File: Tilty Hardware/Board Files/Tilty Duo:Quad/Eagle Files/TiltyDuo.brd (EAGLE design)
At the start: 38.1 x 50.8 mm, 36 parts, among them U1 HMC5883LSMD, U2 HC-09_BREAKOUT, U3 MPL3115A2LGA8, U4 LM2931, U5 MPU-6050

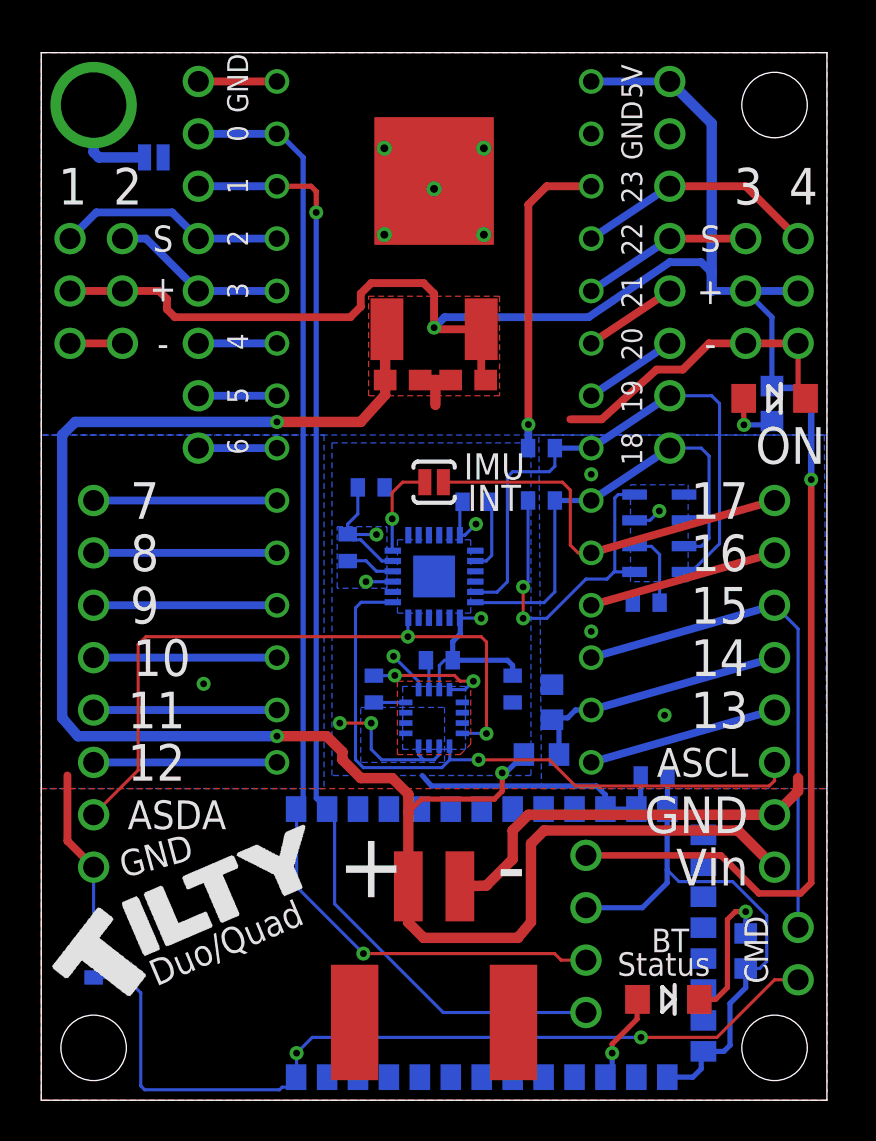
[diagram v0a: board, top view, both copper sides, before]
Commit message: Final prototype Tilty Duo/Quad PCB and BOM
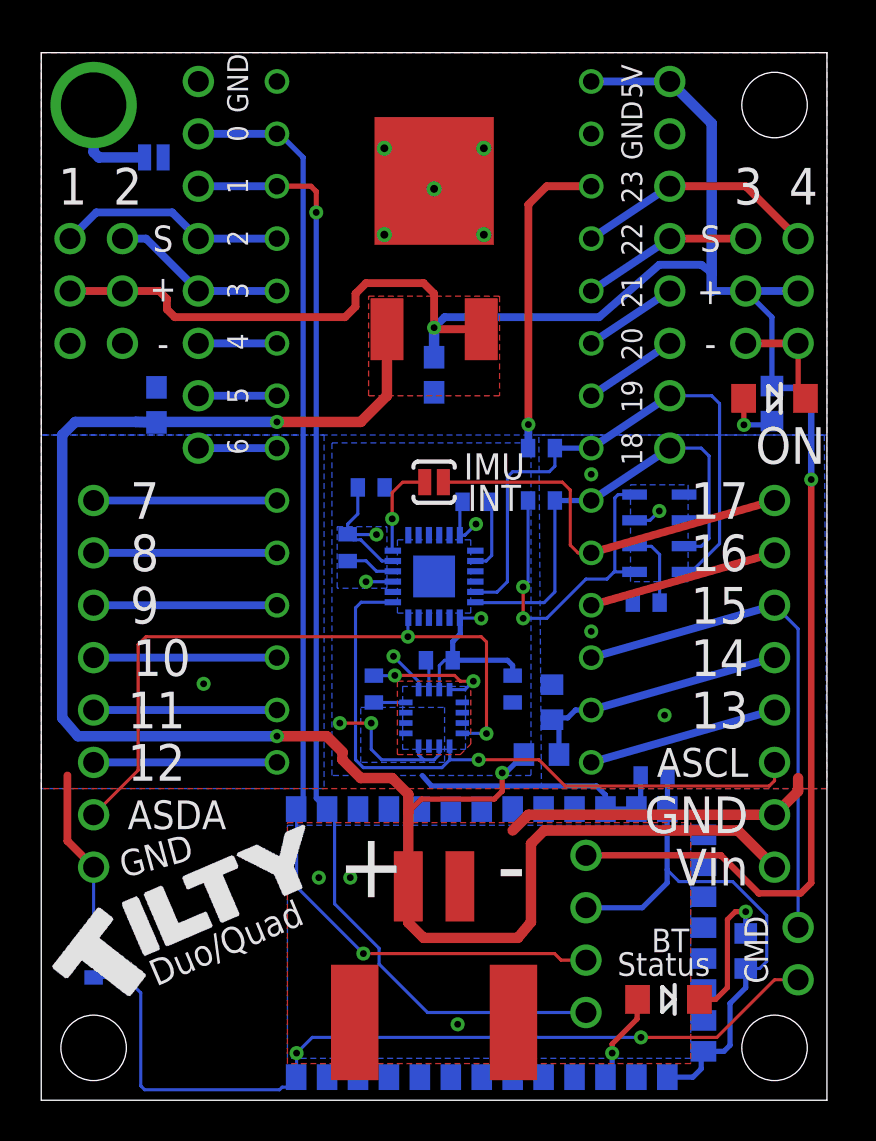
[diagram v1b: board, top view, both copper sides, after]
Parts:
- moved C4 12.0 mm to (5.59, 33.7), flipped to the bottom, turned to 90 degrees
- moved C5 1.67 mm to (19.1, 35.2), flipped to the bottom, turned to 270 degrees
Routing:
- net GND: track 108.3 -> 84.8 mm, vias 15 -> 18
- net 5V: track 102.8 -> 101.6 mm
- net VBATT: track 88.8 -> 90.0 mm
- removed copper zone on layer 1, net N$25

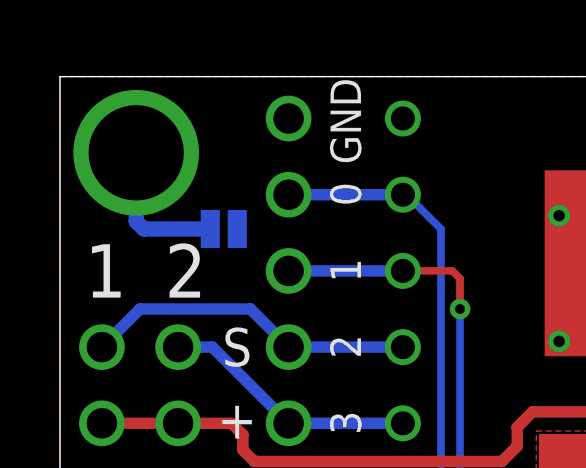
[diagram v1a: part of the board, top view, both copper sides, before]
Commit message: Added Bottom layer solder stencil for Duo/Quad board
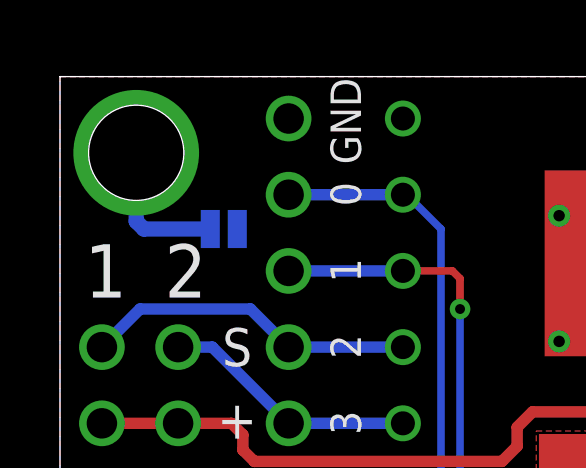
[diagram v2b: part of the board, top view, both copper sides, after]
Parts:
- removed U$1: TEENSY_3.0_OUTER-PINS28-DIP_SOCKET, My Parts:28-DIP
- added U6: HMC5883LSMD, SparkFun:16LPCC
- U1: value HMC5883LSMD -> TEENSY_3.0_OUTER-PINS28-DIP_SOCKET; device SparkFun:16LPCC -> My Parts:28-DIP
- moved U1 14.4 mm to (19.1, 32.9), flipped to the top, turned to 0 degrees
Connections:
- net 5V: now also U1.P$15; no longer U$1.P$15
- net AGND: now also U1.P$16; no longer U$1.P$16
- net AUXCL: now also U6.1; no longer U1.1
- net AUXDA: now also U6.16; no longer U1.16
- net BATT_SENSE: now also U1.P$27; no longer U$1.P$27
- net BT_CMD: now also U1.P$26; no longer U$1.P$26
- net GND: now also U1.P$1, U6.11, U6.9; no longer U$1.P$1, U1.11, U1.9
- net I/O1: now also U1.P$4; no longer U$1.P$4
- net I/O2: now also U1.P$5; no longer U$1.P$5
- net I/O3: now also U1.P$18; no longer U$1.P$18
- net I/O4: now also U1.P$19; no longer U$1.P$19
- net MPU_INT: now also U1.P$24; no longer U$1.P$24
- net N$10: now also U1.P$28; no longer U$1.P$28
- net N$11: now also U6.10; no longer U1.10
- net N$12: now also U1.P$11; no longer U$1.P$11
- net N$13: now also U1.P$12; no longer U$1.P$12
- net N$14: now also U1.P$13; no longer U$1.P$13
- net N$15: now also U1.P$14; no longer U$1.P$14
- net N$18: now also U1.P$20; no longer U$1.P$20
- net N$19: now also U1.P$21; no longer U$1.P$21
- net N$23: now also U1.P$25; no longer U$1.P$25
- net N$5: now also U6.8; no longer U1.8
- net N$6: now also U6.12; no longer U1.12
- net N$7: now also U1.P$6; no longer U$1.P$6
- net N$8: now also U1.P$7; no longer U$1.P$7
- net N$9: now also U1.P$8; no longer U$1.P$8
- net RX1: now also U1.P$2; no longer U$1.P$2
- net RX3: now also U1.P$9; no longer U$1.P$9
- net SCL: now also U1.P$22; no longer U$1.P$22
- net SDA: now also U1.P$23; no longer U$1.P$23
- net TEENSY_3V3: now also U1.P$17, U6.13, U6.2, U6.4; no longer U$1.P$17, U1.13, U1.2, U1.4
- net TX1: now also U1.P$3; no longer U$1.P$3
- net TX3: now also U1.P$10; no longer U$1.P$10
